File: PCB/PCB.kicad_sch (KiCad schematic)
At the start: 109 parts, among them J1 USB_B_Micro, J2 Conn_01x02, Q1 PJA3428, Q2 PJA3428, Q3 AO3401A, SW1 SW_Push, SW2 SW_Push, SW3 SW_Push, SW4 ON/OFF, U1 ESP32-PICO-MINI-02, U2 CP2102N-Axx-xQFN24, U3 TP4056, U4 TPS63070RNMR, U5 BNO080, Y1 32.768 kHz, Y2 32.768 kHz

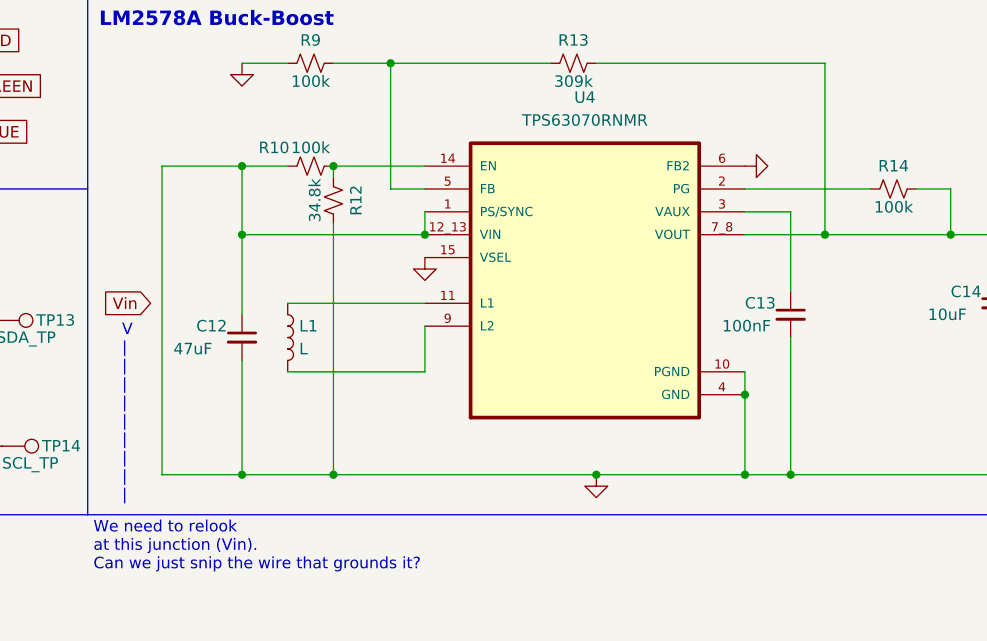
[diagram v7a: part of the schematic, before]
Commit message: buck-boost pcb
layout updated
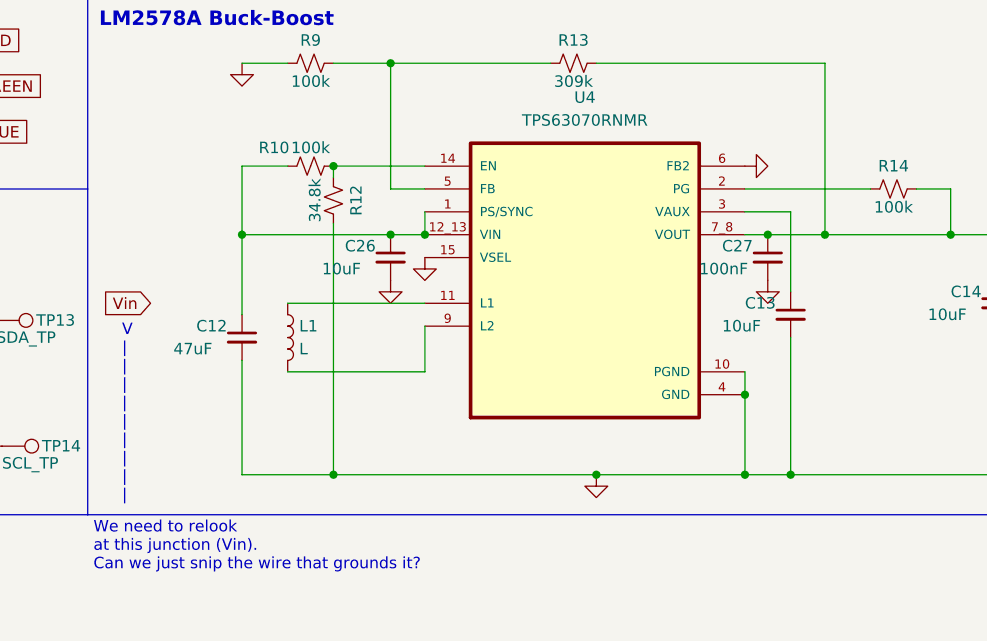
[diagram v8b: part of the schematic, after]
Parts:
- added C26: 10uF, Capacitor_SMD:C_0603_1608Metric, symbol Device:C_Small
- added C27: 100nF, Capacitor_SMD:C_0603_1608Metric, symbol Device:C_Small
- C13: value 100nF -> 10uF
- L1: footprint (none) -> Inductor_SMD:L_0805_2012Metric_Pad1.15x1.40mm_HandSolder
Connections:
- net GND: now also C26.2, C27.2; no longer C12.1, R10.1, U4.1 (PS/SYNC), U4.12_13 (VIN)
- net at C14.1, C17.1, R13.1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: now also C27.1
- new net: C12.1, C26.1, R10.1, U4.1 (PS/SYNC), U4.12_13 (VIN)
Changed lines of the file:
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@@
   (junction (at 280.035 38.1) (diameter 0) (color 0 0 0 0)
   )
+  (junction (at 322.58 116.84) (diameter 0) (color 0 0 0 0)
+  )
   (junction (at 74.93 177.165) (diameter 0) (color 0 0 0 0)
   )
@@
   (junction (at 57.785 196.215) (diameter 0) (color 0 0 0 0)
   )
+  (junction (at 364.49 116.84) (diameter 0) (color 0 0 0 0)
+  )
   (junction (at 164.465 73.025) (diameter 0) (color 0 0 0 0)
   )
@@
   (junction (at 183.515 73.025) (diameter 0) (color 0 0 0 0)
   )
-  (junction (at 306.07 143.51) (diameter 0) (color 0 0 0 0)
-  )
   (junction (at 395.605 47.625) (diameter 0) (color 0 0 0 0)
   )
@@
   (junction (at 389.89 143.51) (diameter 0) (color 0 0 0 0)
   )
-  (junction (at 306.07 109.22) (diameter 0) (color 0 0 0 0)
-  )
   (no_connect (at 179.705 104.775))
   (no_connect (at 31.115 41.275))
@@
     (stroke (width 0) (type default) (color 0 0 0 0))
   )
-  (wire (pts (xy 297.18 109.22) (xy 297.18 143.51))
-    (stroke (width 0) (type default) (color 0 0 0 0))
-  )
   (wire (pts (xy 138.43 102.235) (xy 154.305 102.235))
     (stroke (width 0) (type default) (color 0 0 0 0))
@@
     (stroke (width 0) (type default) (color 0 0 0 0))
   )
-  (wire (pts (xy 306.07 109.22) (xy 297.18 109.22))
-    (stroke (width 0) (type default) (color 0 0 0 0))
-  )
   (polyline (pts (xy 98.425 221.615) (xy 135.255 221.615))
     (stroke (width 0) (type default) (color 0 0 0 0))
@@
     (stroke (width 0) (type default) (color 0 0 0 0))
   )
+  (wire (pts (xy 364.49 116.84) (xy 361.95 116.84))
+    (stroke (width 0) (type default) (color 0 0 0 0))
+  )
   (wire (pts (xy 74.93 177.165) (xy 74.93 177.8))
     (stroke (width 0) (type default) (color 0 0 0 0))
@@
     (stroke (width 0) (type default) (color 0 0 0 0))
   )
-  (wire (pts (xy 370.84 116.84) (xy 361.95 116.84))
+  (wire (pts (xy 370.84 116.84) (xy 364.49 116.84))
     (stroke (width 0) (type default) (color 0 0 0 0))
   )
@@
     (stroke (width 0) (type default) (color 0 0 0 0))
   )
-  (wire (pts (xy 297.18 143.51) (xy 306.07 143.51))
-    (stroke (width 0) (type default) (color 0 0 0 0))
-  )
   (wire (pts (xy 326.39 114.3) (xy 326.39 116.84))
     (stroke (width 0) (type default) (color 0 0 0 0))
@@
     (stroke (width 0) (type default) (color 0 0 0 0))
   )
+  (wire (pts (xy 322.58 116.84) (xy 326.39 116.84))
+    (stroke (width 0) (type default) (color 0 0 0 0))
+  )
   (polyline (pts (xy 13.335 12.7) (xy 103.505 12.7))
     (stroke (width 0) (type default) (color 0 0 0 0))
@@
     (stroke (width 0) (type default) (color 0 0 0 0))
   )
-  (wire (pts (xy 306.07 116.84) (xy 326.39 116.84))
+  (wire (pts (xy 306.07 116.84) (xy 322.58 116.84))
     (stroke (width 0) (type default) (color 0 0 0 0))
   )
@@
       (effects (font (size 1.27 1.27)) (justify left))
     )
-    (property "Value" "100nF" (id 1) (at 359.41 127 0)
+    (property "Value" "10uF" (id 1) (at 359.41 127 0)
       (effects (font (size 1.27 1.27)) (justify left))
     )
@@
     (pin "2")
   )
+  (symbol (lib_id "Device:C_Small") (at 322.58 119.38 0) (unit 1)
+    (in_bom yes) (on_board yes)
+    (property "Reference" "C26" (id 0) (at 317.5 118.11 0)
+      (effects (font (size 1.27 1.27)) (justify left))
+    )
+    (property "Value" "10uF" (id 1) (at 314.96 120.65 0)
+      (effects (font (size 1.27 1.27)) (justify left))
+    )
+    (property "Footprint" "Capacitor_SMD:C_0603_1608Metric" (id 2) (at 322.58 119.38 0)
+      (effects (font (size 1.27 1.27)) hide)
+    )
+    (property "Datasheet" "~" (id 3) (at 322.58 119.38 0)
+      (effects (font (size 1.27 1.27)) hide)
+    )
+    (pin "1")
+    (pin "2")
+  )
   (symbol (lib_id "Device:LED_Small") (at 242.57 67.945 180) (unit 1)
     (in_bom yes) (on_board yes) (fields_autoplaced)
@@
     (pin "1")
   )
+  (symbol (lib_id "power:GND") (at 364.49 121.92 0) (unit 1)
+    (in_bom yes) (on_board yes) (fields_autoplaced)
+    (property "Reference" "#PWR030" (id 0) (at 364.49 128.27 0)
+      (effects (font (size 1.27 1.27)) hide)
+    )
+    (property "Value" "GND" (id 1) (at 364.49 126.3634 0)
+      (effects (font (size 1.27 1.27)) hide)
+    )
+    (property "Footprint" "" (id 2) (at 364.49 121.92 0)
+      (effects (font (size 1.27 1.27)) hide)
+    )
+    (property "Datasheet" "" (id 3) (at 364.49 121.92 0)
+      (effects (font (size 1.27 1.27)) hide)
+    )
+    (pin "1")
+  )
+  (symbol (lib_id "Device:C_Small") (at 364.49 119.38 0) (unit 1)
+    (in_bom yes) (on_board yes)
+    (property "Reference" "C27" (id 0) (at 359.41 118.11 0)
+      (effects (font (size 1.27 1.27)) (justify left))
+    )
+    (property "Value" "100nF" (id 1) (at 356.87 120.65 0)
+      (effects (font (size 1.27 1.27)) (justify left))
+    )
+    (property "Footprint" "Capacitor_SMD:C_0603_1608Metric" (id 2) (at 364.49 119.38 0)
+      (effects (font (size 1.27 1.27)) hide)
+    )
+    (property "Datasheet" "~" (id 3) (at 364.49 119.38 0)
+      (effects (font (size 1.27 1.27)) hide)
+    )
+    (pin "1")
+    (pin "2")
+  )
   (symbol (lib_id "Device:L") (at 311.15 128.27 0) (unit 1)
     (in_bom yes) (on_board yes) (fields_autoplaced)
@@
       (effects (font (size 1.27 1.27)) (justify left))
     )
-    (property "Footprint" "" (id 2) (at 311.15 128.27 0)
+    (property "Footprint" "Inductor_SMD:L_0805_2012Metric_Pad1.15x1.40mm_HandSolder" (id 2) (at 311.15 128.27 0)
       (effects (font (size 1.27 1.27)) hide)
     )
@@
     (pin "9")
   )
+  (symbol (lib_id "power:GND") (at 322.58 121.92 0) (unit 1)
+    (in_bom yes) (on_board yes) (fields_autoplaced)
+    (property "Reference" "#PWR022" (id 0) (at 322.58 128.27 0)
+      (effects (font (size 1.27 1.27)) hide)
+    )
+    (property "Value" "GND" (id 1) (at 322.58 126.3634 0)
+      (effects (font (size 1.27 1.27)) hide)
+    )
+    (property "Footprint" "" (id 2) (at 322.58 121.92 0)
+      (effects (font (size 1.27 1.27)) hide)
+    )
+    (property "Datasheet" "" (id 3) (at 322.58 121.92 0)
+      (effects (font (size 1.27 1.27)) hide)
+    )
+    (pin "1")
+  )
   (symbol (lib_id "Device:R_Small_US") (at 47.625 170.815 90) (unit 1)
     (in_bom yes) (on_board yes) (fields_autoplaced)
@@
       (reference "#PWR021") (unit 1) (value "GND") (footprint "")
     )
+    (path "/f7fb7a7c-0192-466c-aa4c-eac5b4663929"
+      (reference "#PWR022") (unit 1) (value "GND") (footprint "")
+    )
     (path "/060bc8e9-31b5-46c1-8e34-75b7fc414520"
       (reference "#PWR023") (unit 1) (value "GND") (footprint "")
@@
       (reference "#PWR029") (unit 1) (value "GND") (footprint "")
     )
+    (path "/c1021e96-c8c5-42b1-9993-ab46c5556871"
+      (reference "#PWR030") (unit 1) (value "GND") (footprint "")
+    )
     (path "/25589d4d-c6ec-4187-b03e-68eac9ce0149"
       (reference "#PWR031") (unit 1) (value "+3.3V") (footprint "")
@@
     )
     (path "/1064231c-bfd3-489f-ae80-b5249537604d"
-      (reference "C13") (unit 1) (value "100nF") (footprint "Capacitor_SMD:C_0603_1608Metric")
+      (reference "C13") (unit 1) (value "10uF") (footprint "Capacitor_SMD:C_0603_1608Metric")
     )
     (path "/1efd981a-b294-4f8f-8a3b-cd723ec3f3c5"
@@
       (reference "C25") (unit 1) (value "10uF") (footprint "Capacitor_SMD:C_0603_1608Metric")
     )
+    (path "/1530e7e9-42a0-4dee-a1a3-162bef1ffd20"
+      (reference "C26") (unit 1) (value "10uF") (footprint "Capacitor_SMD:C_0603_1608Metric")
+    )
+    (path "/c2952636-7ad4-4c20-8de3-ed7e9fecf3f5"
+      (reference "C27") (unit 1) (value "100nF") (footprint "Capacitor_SMD:C_0603_1608Metric")
+    )
     (path "/8de632ee-0d20-40ed-ae11-2bd51fcd40ad"
       (reference "D1") (unit 1) (value "PRTR5V0U2X") (footprint "Package_TO_SOT_SMD:SOT-143")
@@
     )
     (path "/c386aa6a-54a9-4a0e-9ad5-3e2e9aeae025"
-      (reference "L1") (unit 1) (value "L") (footprint "")
+      (reference "L1") (unit 1) (value "L") (footprint "Inductor_SMD:L_0805_2012Metric_Pad1.15x1.40mm_HandSolder")
     )
     (path "/cef27ab4-b73f-410e-8967-9f4b41c610a5"
